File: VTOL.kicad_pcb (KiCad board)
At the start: 4 copper layers, 124.9 x 103.9 mm, 45 parts, among them J1 Conn_01x06_Pin, J2 Conn_01x06_Pin, J3 Conn_01x04_Pin, J5 USB_C_Receptacle_USB2.0_16P, J6 Conn_01x02_Pin, J7 Conn_01x06_Pin, SW1 RESET, SW2 RESET, U1 DS18B20, U2 SEN0460, U3 Si7021-A20, U4 ESP32-S3-WROOM-1, U5 USBLC6-2SC6, U6 AMS1117-3.3

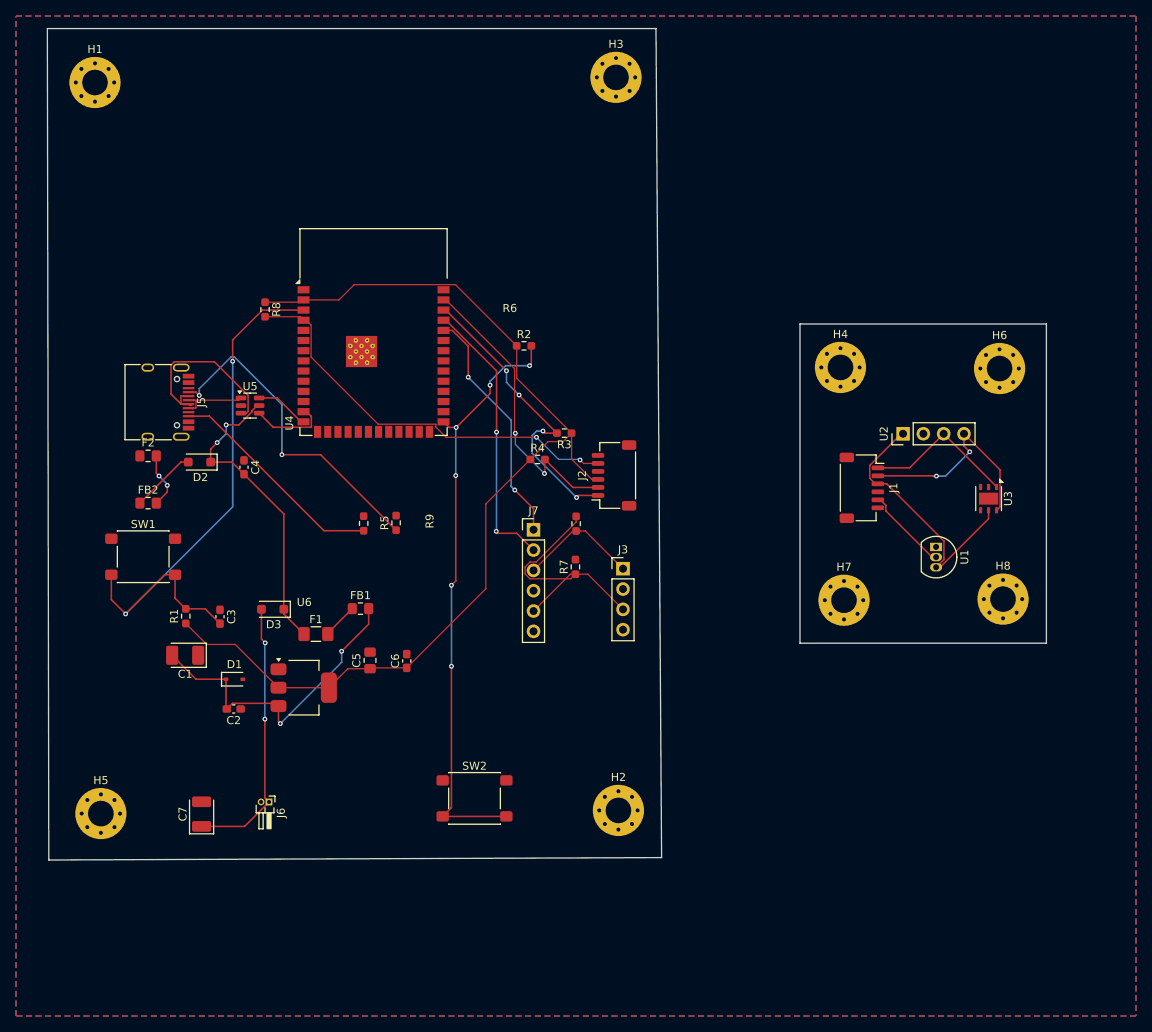
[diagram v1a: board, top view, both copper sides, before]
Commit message: Rework power, sensors and PCB layout; add DigiKey BOM
- Power: 4S LiPo input (J6 -> F2 polyfuse -> R-78E 5V buck) with hot-plug
  damping cap (C13), USB/battery select switch SW3, AP7361C LDO with
  ceramic caps.
- Sensors: SEN66 (J8) replaces SEN0460/Si7021/DS18B20; two I2C headers.
- Pi link reduced to a 3-pin UART; camera pass-through removed.
- PCB: re-placed by function, 4-layer (GND + 3V3 planes), rerouted,
  DigiKey footprint swaps in the VTOL_parts library, sub-board removed.
- Schematic tidy: decoupling caps grouped on shared rails; drop redundant
  C2/C6 0.1u caps.
- BOM_digikey.csv for DigiKey BOM Manager.

Co-Authored-By: Claude Opus 5.5 <noreply@anthropic.com>
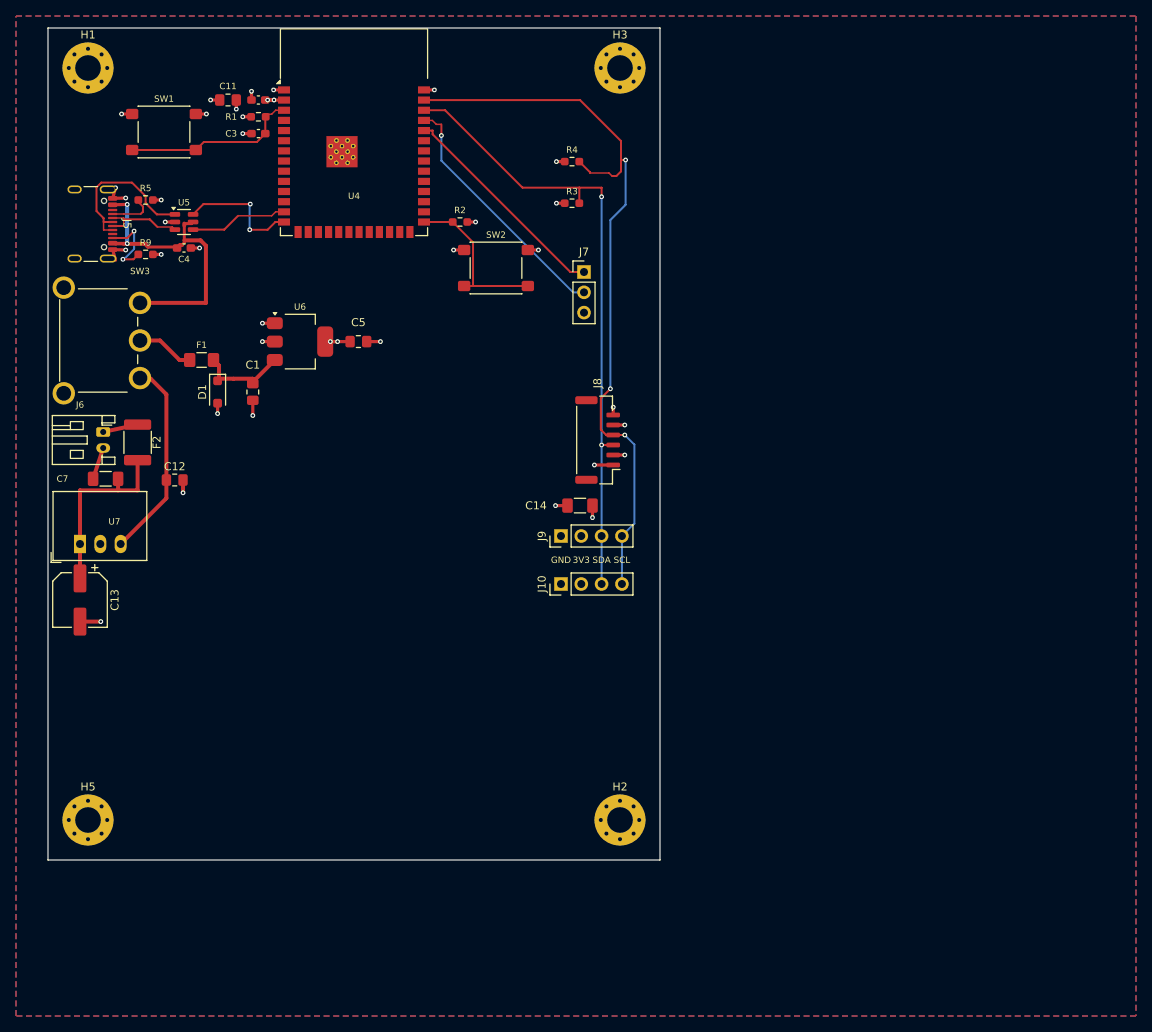
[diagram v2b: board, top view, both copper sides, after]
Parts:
- removed C2, C6: 0.1u, Capacitor_SMD:C_0603_1608Metric_Pad1.08x0.95mm_HandSolder
- removed D2, D3: 1A, Diode_SMD:D_SOD-123F
- removed FB1, FB2: FerriteBead, Inductor_SMD:L_0805_2012Metric_Pad1.15x1.40mm_HandSolder
- removed H4, H6, H7, H8: MountingHole, MountingHole:MountingHole_3.2mm_M3_Pad_Via
- removed J1, J2: Conn_01x06_Pin, Connector_JST:JST_SH_SM06B-SRSS-TB_1x06-1MP_P1.00mm_Horizontal
- removed J3: Conn_01x04_Pin, Connector_PinHeader_2.54mm:PinHeader_1x04_P2.54mm_Vertical
- removed R6, R7, R8: 4.7k, Resistor_SMD:R_0603_1608Metric_Pad0.98x0.95mm_HandSolder
- removed U1: DS18B20, Package_TO_SOT_THT:TO-92_Inline
- removed U2: SEN0460, Connector_PinHeader_2.54mm:PinHeader_1x04_P2.54mm_Vertical
- removed U3: Si7021-A20, Package_DFN_QFN:DFN-6-1EP_3x3mm_P1mm_EP1.5x2.4mm
- added C10: 0.1u 50V, Capacitor_SMD:C_0603_1608Metric_Pad1.08x0.95mm_HandSolder, F.Cu at (135.3, 25.5)
- added C11: 10u 25V, Capacitor_SMD:C_0805_2012Metric_Pad1.18x1.45mm_HandSolder, F.Cu at (131.5, 25.5)
- added C12: 10u 25V, Capacitor_SMD:C_0805_2012Metric_Pad1.18x1.45mm_HandSolder, F.Cu at (124.8, 73.0)
- added C13: 47u 35V, Capacitor_SMD:CP_Elec_6.3x5.8, F.Cu at (113.0, 88.0)
- added C14: 47u 10V, Capacitor_SMD:C_1206_3216Metric_Pad1.33x1.80mm_HandSolder, F.Cu at (175.5, 76.2)
- added J10: I2C header, Connector_PinHeader_2.54mm:PinHeader_1x04_P2.54mm_Vertical, F.Cu at (173.1, 86.0)
- added J8: SEN66, Connector_JST:JST_GH_BM06B-GHS-TBT_1x06-1MP_P1.25mm_Vertical, F.Cu at (177.7, 68.0)
- added J9: I2C header, Connector_PinHeader_2.54mm:PinHeader_1x04_P2.54mm_Vertical, F.Cu at (173.1, 80.0)
- added SW3: SW_SPDT, VTOL_parts:SW_Slide_SPDT_RightAngle_CK_1101M2S3AQE2, F.Cu at (120.5, 55.6)
- added U7: R-78E5.0-1.0, Converter_DCDC:Converter_DCDC_RECOM_R-78E-0.5_THT, F.Cu at (113.0, 81.0)
- C1: value 100u -> 10u 25V; footprint Capacitor_Tantalum_SMD:CP_EIA-3528-21_Kemet-B_HandSolder -> Capacitor_SMD:C_0805_2012Metric_Pad1.18x1.45mm_HandSolder
- C3: value 0.1u -> 1u 50V
- C4: value 0.1u -> 0.1u 50V
- C5: value 10u -> 10u 25V
- C7: value 100u -> 10u 50V; footprint Capacitor_Tantalum_SMD:CP_EIA-3528-21_Kemet-B -> Capacitor_SMD:C_1206_3216Metric_Pad1.33x1.80mm_HandSolder
- D1: value PTVS5V0Z1USK -> SMF5.0A; footprint Diode_SMD:D_SOD-323 -> Diode_SMD:D_SOD-123F
- F2: value 500mA -> 0.75A 24V; footprint Fuse:Fuse_0805_2012Metric_Pad1.15x1.40mm_HandSolder -> Fuse:Fuse_1812_4532Metric_Pad1.30x3.40mm_HandSolder
- J5: footprint Connector_USB:USB_C_Receptacle_HRO_TYPE-C-31-M-12 -> VTOL_parts:USB_C_Receptacle_GCT_USB4105-GF-A_16P_TopMnt_Horizontal_S1
- J6: footprint Connector_PinHeader_1.00mm:PinHeader_1x02_P1.00mm_Horizontal -> Connector_JST:JST_PH_S2B-PH-K_1x02_P2.00mm_Horizontal
- J7: value Conn_01x06_Pin -> Pi UART; footprint Connector_PinHeader_2.54mm:PinHeader_1x06_P2.54mm_Vertical -> Connector_PinHeader_2.54mm:PinHeader_1x03_P2.54mm_Vertical
- SW2: value RESET -> BOOT
- U4: footprint RF_Module:ESP32-S3-WROOM-1 -> VTOL_parts:ESP32-S3-WROOM-1_Via0.3mm
- U6: value AMS1117-3.3 -> AP7361C-33ER-13
- moved SW2 66.4 mm to (165.0, 46.5)
- moved R1 63.1 mm to (135.3, 27.6), turned to 0 degrees
- moved C3 60.6 mm to (135.3, 29.7), turned to 0 degrees
- moved SW1 53.2 mm to (123.5, 29.5)
- moved R5 51.1 mm to (121.2, 38.0), turned to 0 degrees
- moved J6 50.7 mm to (115.9, 67.0)
- moved C7 43.6 mm to (116.2, 72.8), turned to 180 degrees
- moved R9 43.3 mm to (121.2, 44.8), turned to 0 degrees
- moved U6 43.3 mm to (140.5, 55.7)
- moved C5 39.9 mm to (147.8, 55.7), turned to 0 degrees
- moved R4 37.5 mm to (174.5, 33.2)
- moved F1 37.1 mm to (128.2, 58.0)
- moved D1 36.0 mm to (130.2, 62.0), turned to -90 degrees
- moved C1 34.0 mm to (134.6, 62.0), turned to -90 degrees
- moved J7 32.8 mm to (176.0, 47.0)
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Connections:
- net /PI_RX renamed /ESP_RX
- net /PI_TX renamed /ESP_TX
- C1 pad 1: GND -> /5V_FUSED
- C1 pad 2: Net-(D1-K) -> GND
- C4 pad 2: +5V -> VBUS
- D1 pad 1: Net-(D1-K) -> /5V_FUSED
- F1 pad 2: Net-(F1-Pad2) -> /5V_FUSED
- F2 pad 1: Net-(F2-Pad1) -> /BATT_IN
- F2 pad 2: Net-(F2-Pad2) -> +BATT
- J5 pad A4: Net-(F2-Pad1) -> VBUS
- J5 pad A9: Net-(F2-Pad1) -> VBUS
- J5 pad B4: Net-(F2-Pad1) -> VBUS
- J5 pad B9: Net-(F2-Pad1) -> VBUS
- J6 pad 1: +BATT -> /BATT_IN
- J7 pad 3: /CAM_SDA -> GND
- U4 pad 4: /TEMP_DATA -> unconnected-(U4-IO4-Pad4)
- U5 pad 5: +5V -> VBUS
- U6 pad 3: Net-(D1-K) -> /5V_FUSED
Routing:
- net +3.3V: track 161.6 -> 18.8 mm, vias 0 -> 13
- net /TEMP_DATA: track 62.6 -> 0.00 mm, vias 2 -> 0
- net /BOOT: track 75.0 -> 20.6 mm, vias 6 -> 0
- net /EN: track 73.9 -> 22.4 mm, vias 2 -> 0
- net GND: track 0.00 -> 40.7 mm, vias 0 -> 25
- net VBUS: track 0.00 -> 39.9 mm, vias 0 -> 2
- net Net-(D1-K): track 39.9 -> 0.00 mm, vias 2 -> 0
- net /CC1: track 41.2 -> 5.61 mm, vias 2 -> 0
- net /PI_3V3: track 32.0 -> 0.00 mm
- net /SCL: track 63.9 -> 95.4 mm, vias 4 -> 3
- net +5V: track 38.5 -> 7.22 mm, vias 2 -> 0
- net /BATT_5V: track 0.00 -> 25.2 mm
- net /SDA: track 57.1 -> 79.1 mm, vias 4 -> 2
- net /CC2: track 27.8 -> 9.38 mm, vias 0 -> 2
- net /CAM_SDA: track 15.2 -> 0.00 mm
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- added copper zone on In2.Cu, net +3.3V
- added copper zone on In1.Cu, net GND
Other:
- board size 124.9 x 103.9 mm -> 76.5 x 104 mm
- board text added: "3V3"
- board text added: "GND"
- board text added: "SCL"
- board text added: "SDA"
